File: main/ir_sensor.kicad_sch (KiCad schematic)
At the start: 2 parts, among them Q1 LTR-209

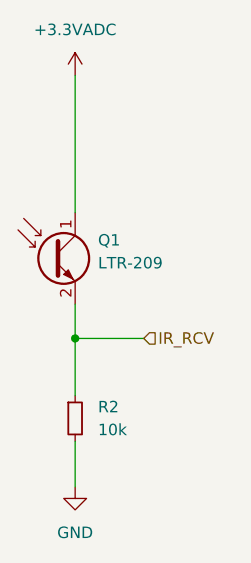
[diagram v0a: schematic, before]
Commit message: feat: update main board
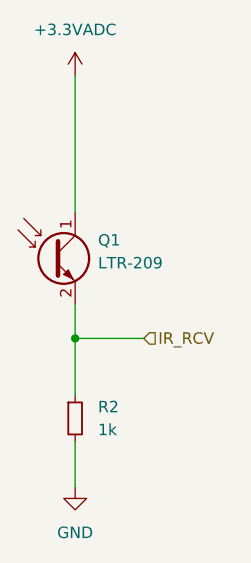
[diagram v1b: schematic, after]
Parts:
- R2: value 10k -> 1k
